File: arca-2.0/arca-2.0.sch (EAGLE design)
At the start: 204 parts, among them IC1 MCP6N11R, IC2 MCP6N11R, IC3 MCP6N11R, IC4 MCP6N11R, IC5 LM324D, IC6 LM324D, SW1 1101M2S3CQE2, SW2 1101M2S3CQE2, T1 FQP30N06L, T2 FQP30N06L, T3 FQP30N06L, T4 FQP30N06L, T5 FQP30N06L, T6 FQP30N06L, X1 2540-5

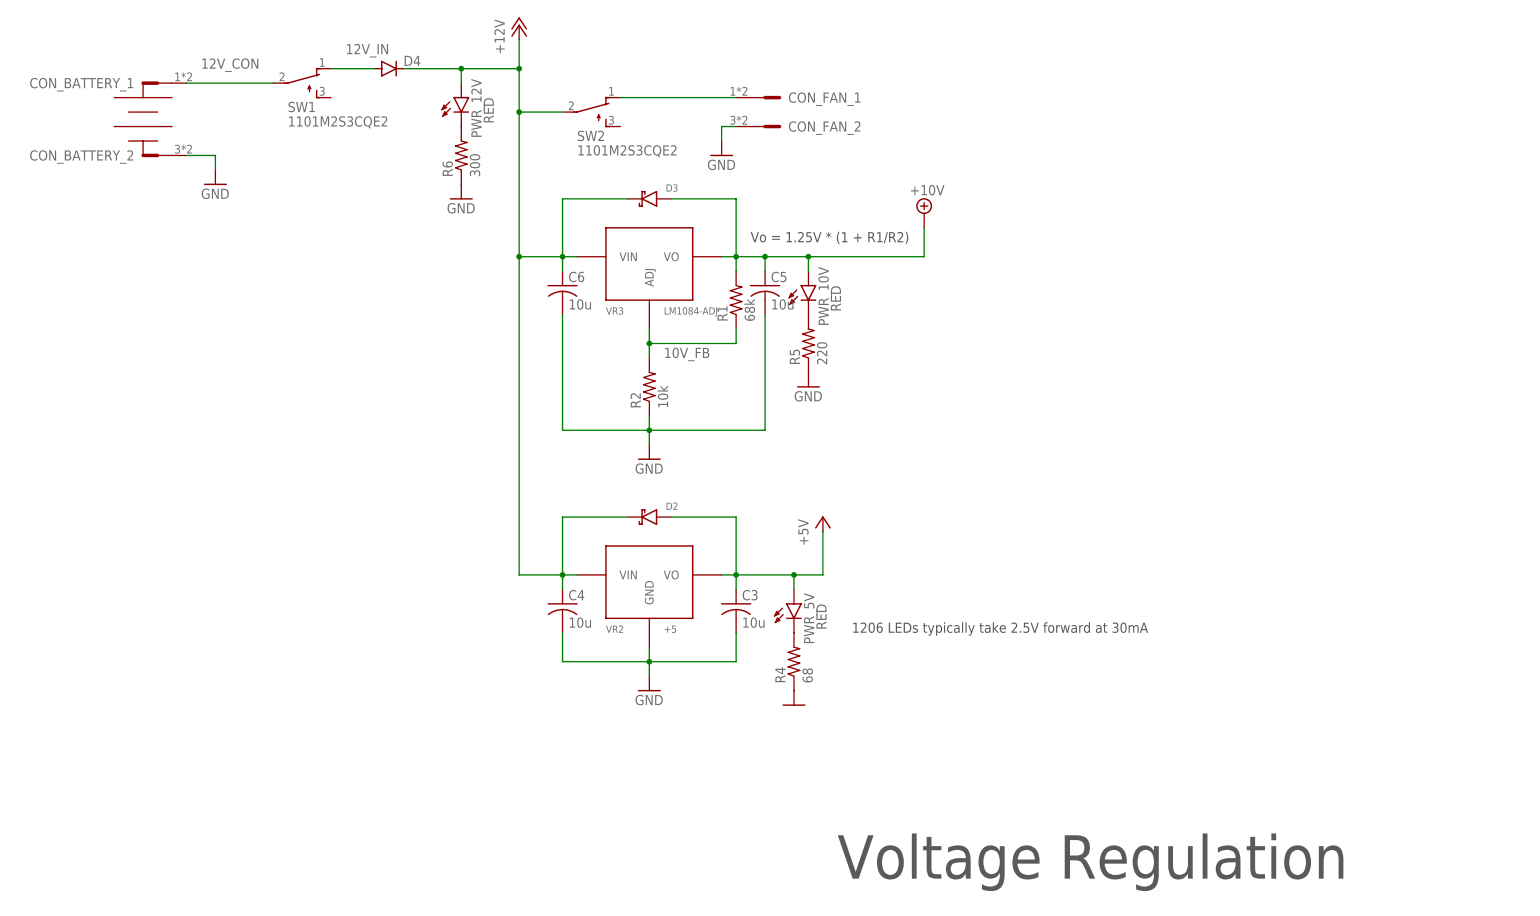
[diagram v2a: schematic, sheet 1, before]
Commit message: add connector for router
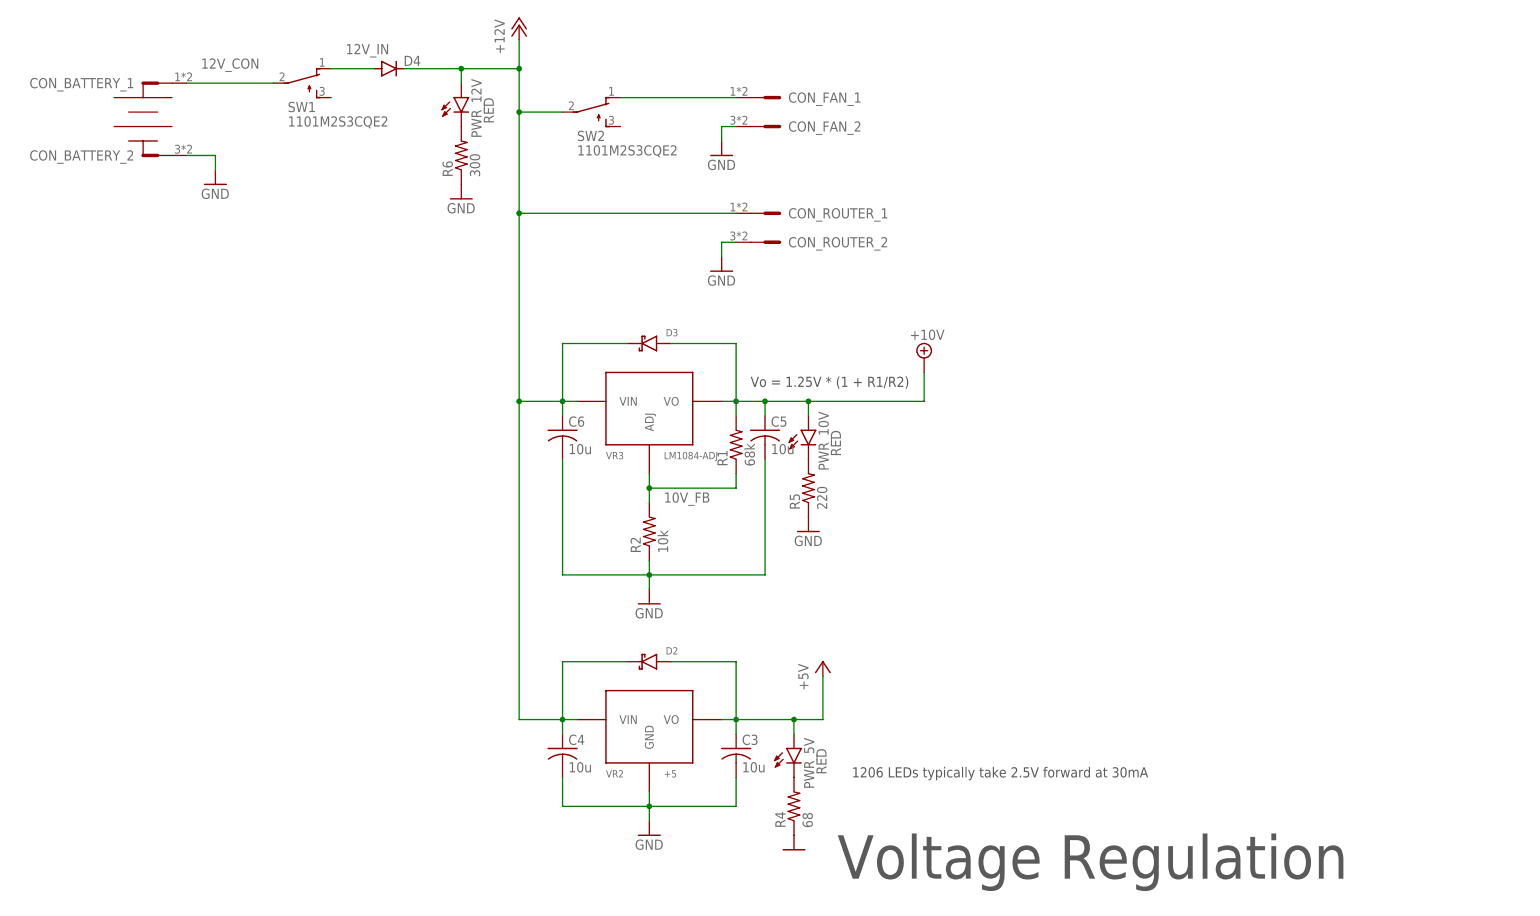
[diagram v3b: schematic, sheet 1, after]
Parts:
- added CON_ROUTER: LPTA-2POS, con-phoenix-5mm:LPTA-2POS
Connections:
- net +12V: now also CON_ROUTER_1.SK
- net GND: now also CON_ROUTER_2.SK
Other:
- moved on the sheet: C3, C4, C5, C6, D2, D3, PWR_10V, PWR_5V, R1, R2, R4, R5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

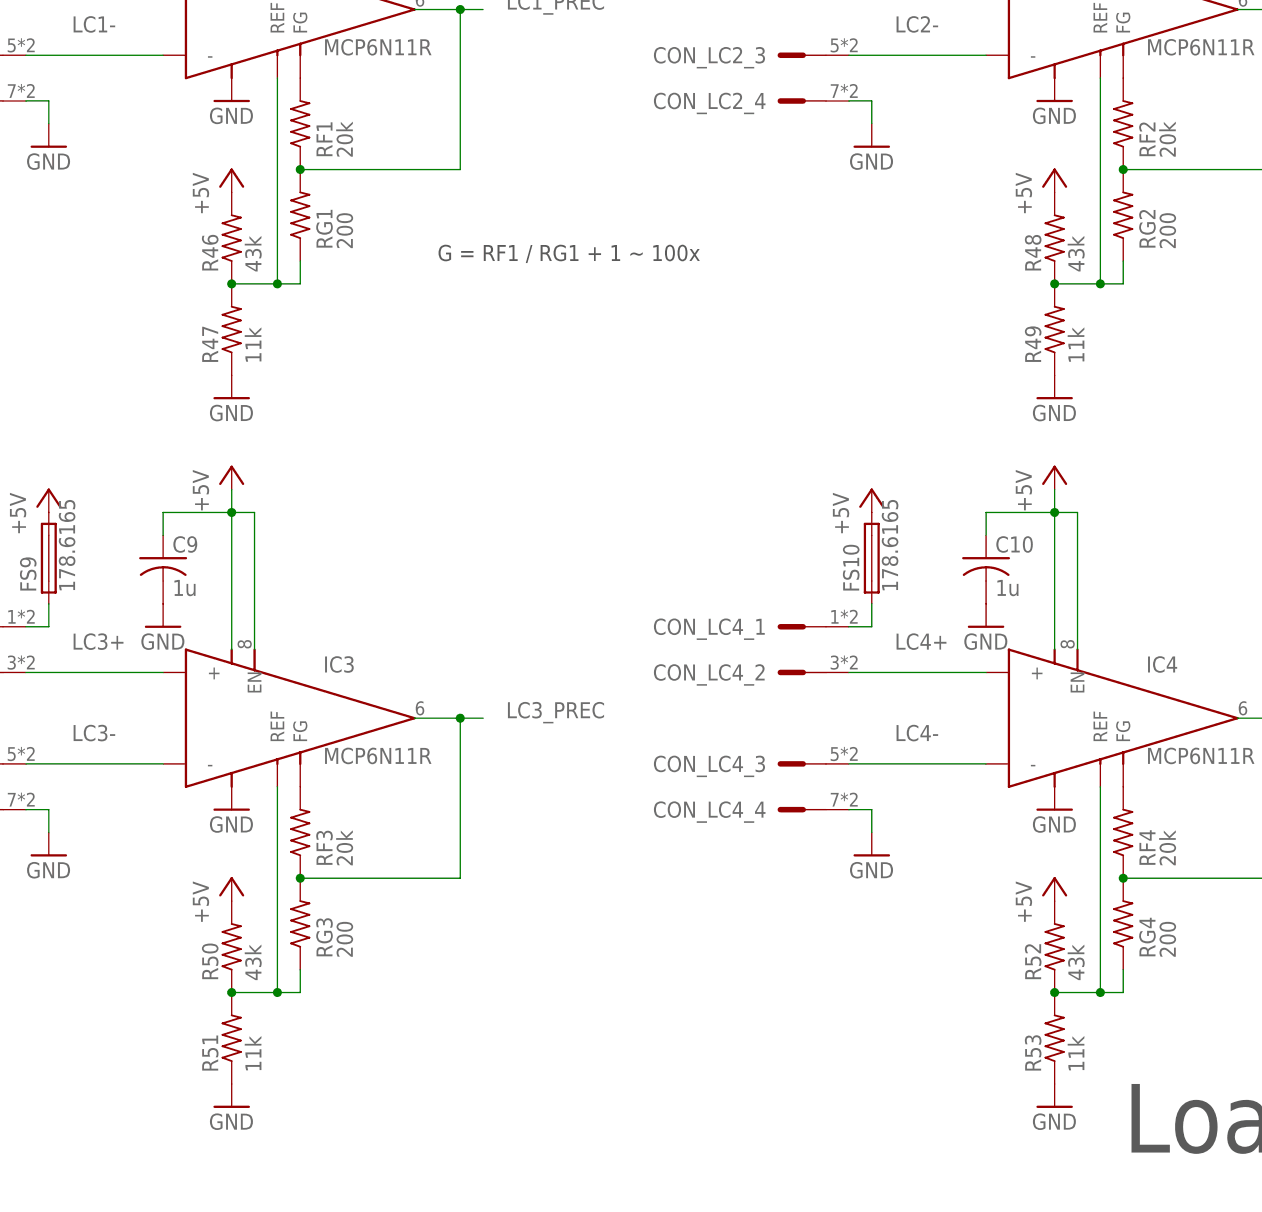
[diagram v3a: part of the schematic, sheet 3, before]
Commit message: move to potentiometers for load cells
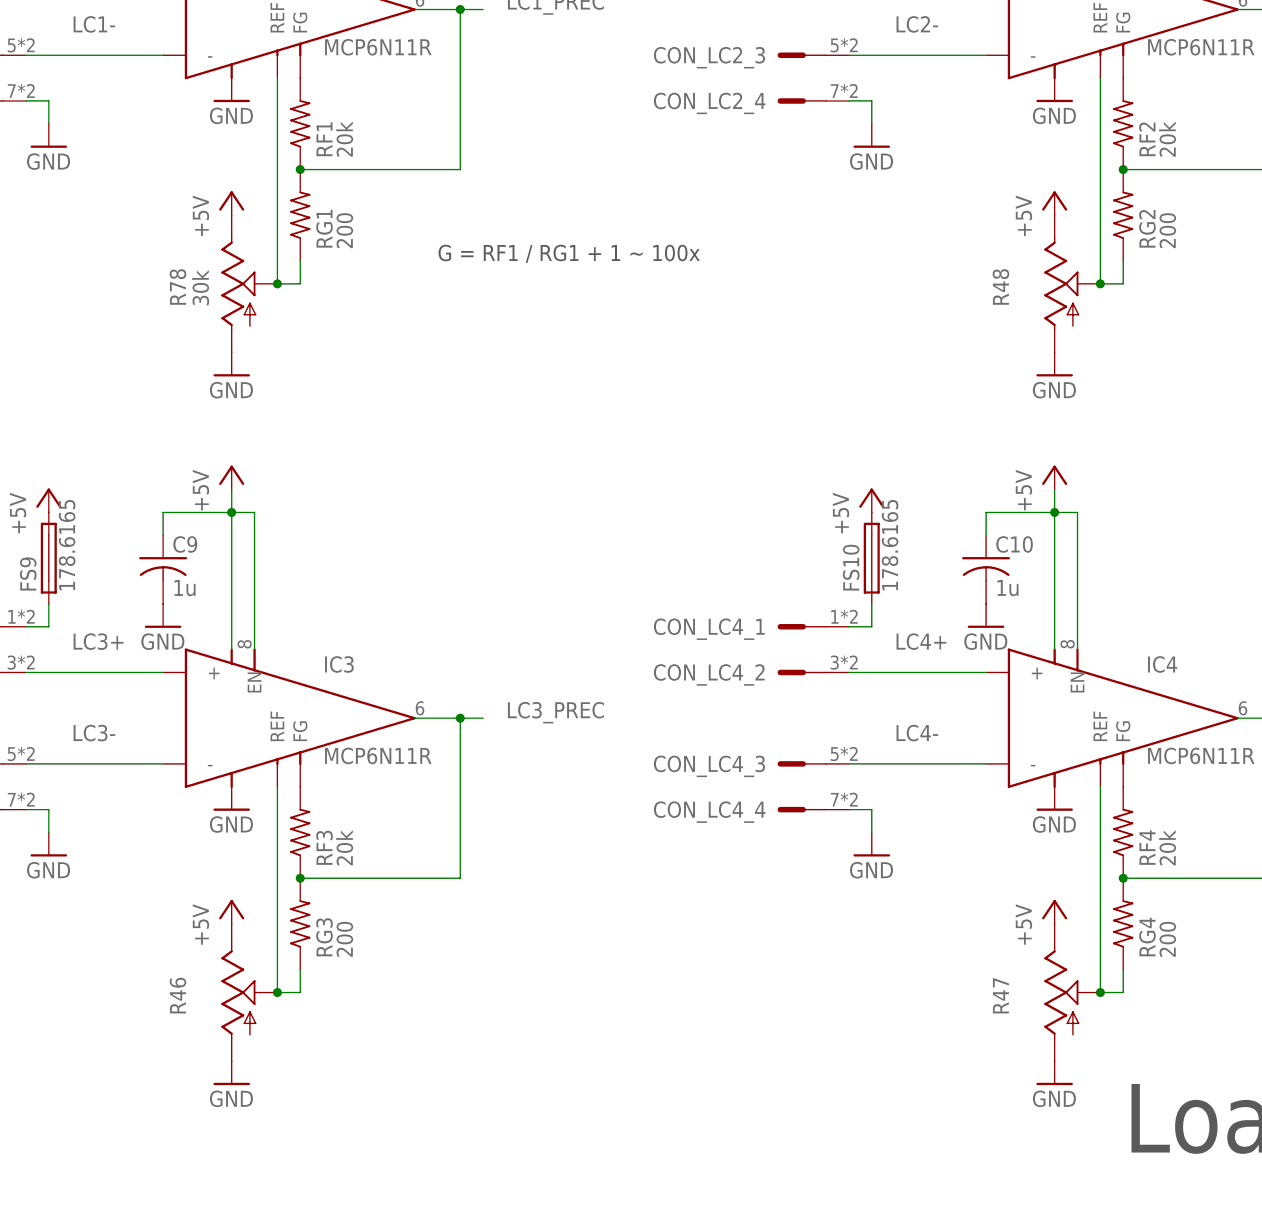
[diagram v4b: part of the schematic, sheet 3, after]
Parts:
- removed R49, R51, R53: 11k, rcl:R-US_R1206
- removed R50, R52: 43k, rcl:R-US_R1206
- added R78: 30k, pot:TRIM_US-S64W
- R46, R48: value 43k -> (none); device rcl:R-US_R1206 -> pot:TRIM_US-S64W
- R47: value 11k -> (none); device rcl:R-US_R1206 -> pot:TRIM_US-S64W
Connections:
- net +5V: now also R46.E, R47.E, R48.E, R78.E; no longer R46.2, R48.2, R50.2, R52.2
- net GND: now also R46.A, R47.A, R48.A, R78.A; no longer R47.1, R49.1, R51.1, R53.1
- net N$17: now also R48.S; no longer R48.1, R49.2
- net N$2: now also R78.S; no longer R46.1, R47.2
- net N$28: now also R47.S; no longer R52.1, R53.2
- net N$37: now also R46.S; no longer R50.1, R51.2

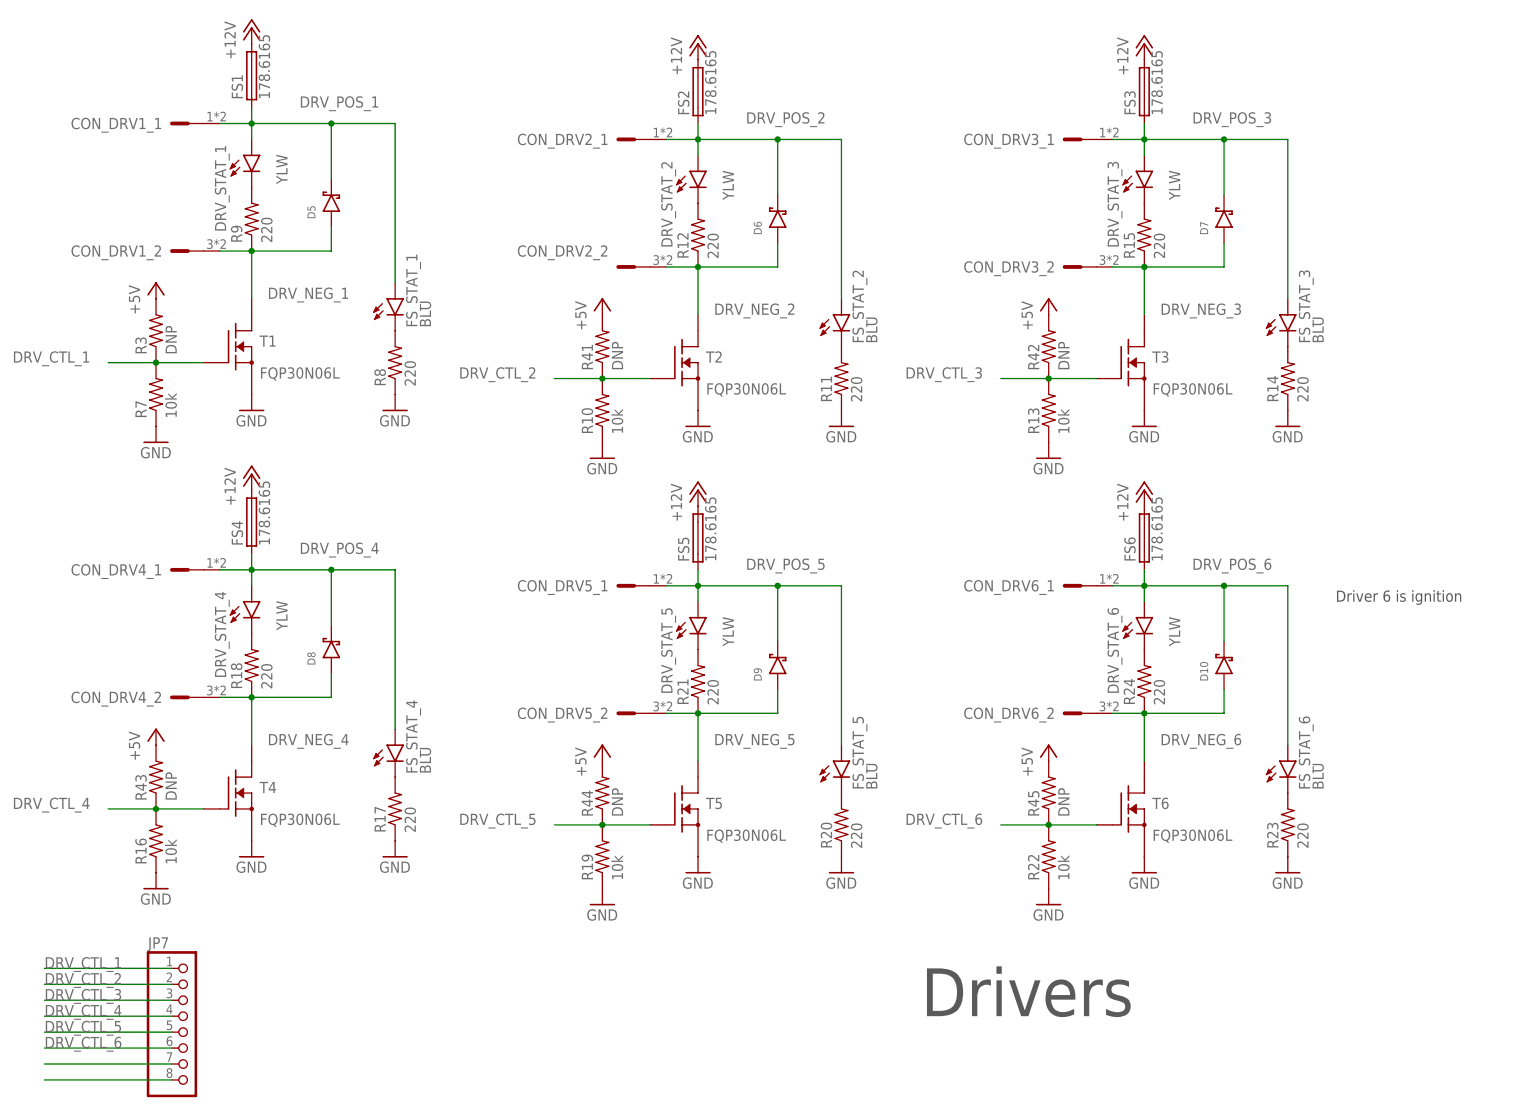
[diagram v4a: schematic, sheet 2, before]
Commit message: cheaper fuses
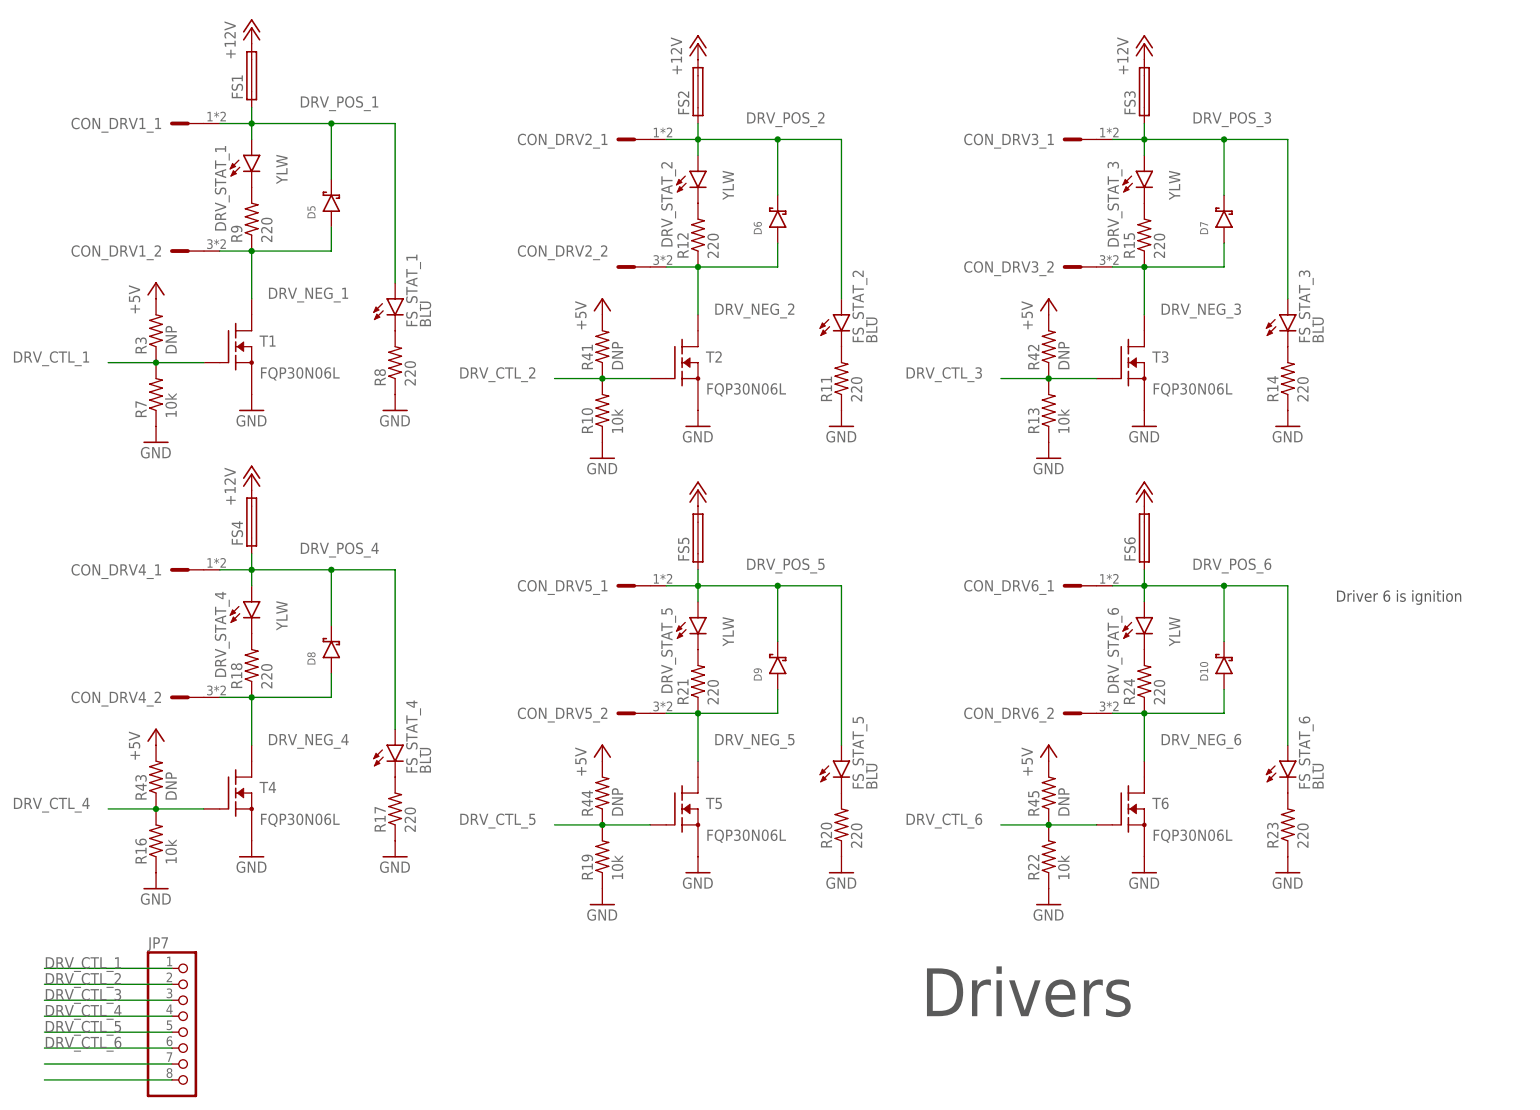
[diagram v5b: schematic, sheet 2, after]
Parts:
- FS1, FS10, FS11, FS12, FS13, FS14, FS15, FS16, FS17, FS18, FS2, FS3, FS4, FS5, FS6, FS7, FS8, FS9: value 178.6165 -> HOLDER_3588-20; device fuse-holder-littlefuse:178.6165 -> fuse-keystone:HOLDER_3588-20
